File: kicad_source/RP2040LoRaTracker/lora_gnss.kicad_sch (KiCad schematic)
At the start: 16 parts, among them U2 Ai-Thinker-Ra-01, U3 NEO-M8N, U5 24LC32

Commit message: started layout
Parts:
- U5: footprint (none) -> Package_SO:TSSOP-8_4.4x3mm_P0.65mm
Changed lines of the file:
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@@
 			)
 		)
-		(property "Footprint" ""
+		(property "Footprint" "Package_SO:TSSOP-8_4.4x3mm_P0.65mm"
 			(at 41.91 128.27 0)
 			(effects

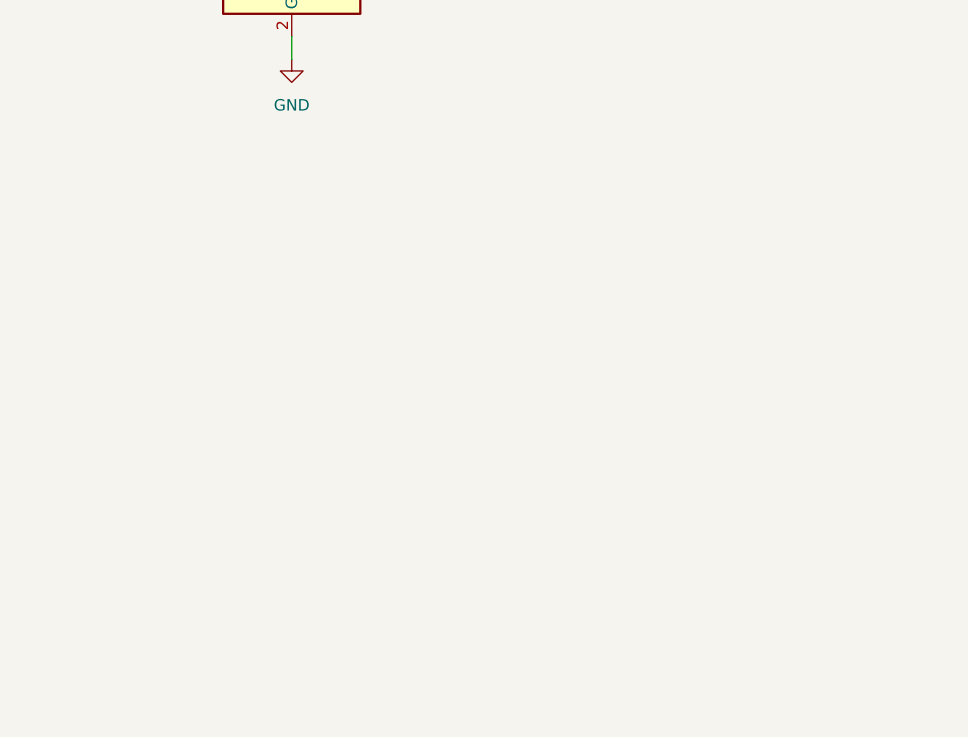
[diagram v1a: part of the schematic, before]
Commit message: added BME280 and quiic connector
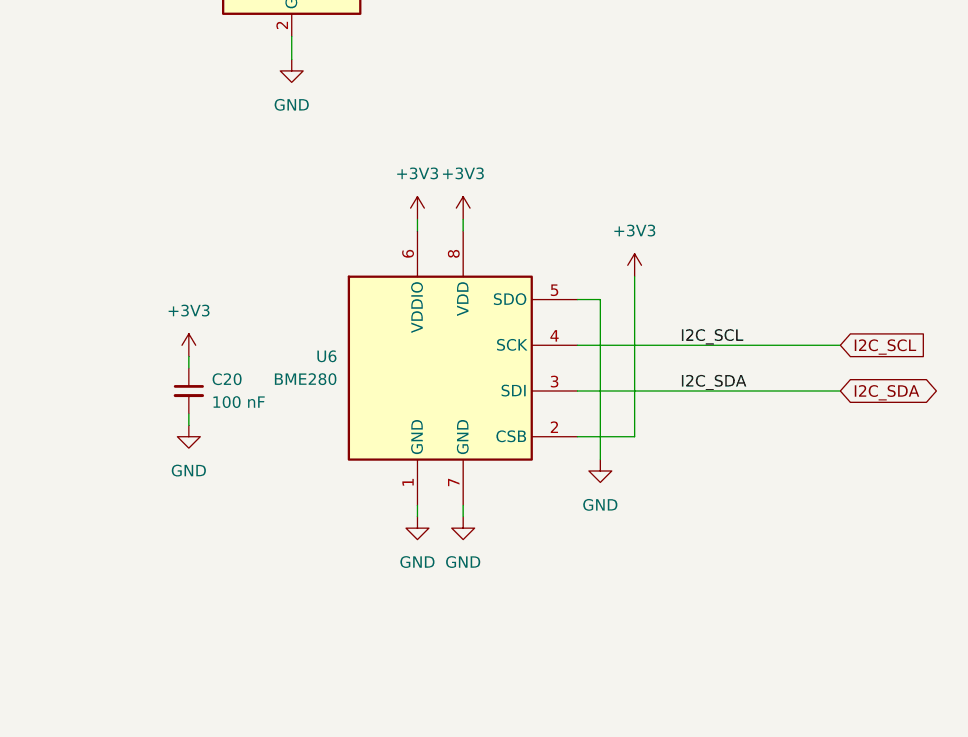
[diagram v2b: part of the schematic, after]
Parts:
- added C20: 100 nF, Capacitor_SMD:C_0603_1608Metric, symbol Device:C_Small
- added U6: BME280, Package_LGA:Bosch_LGA-8_2.5x2.5mm_P0.65mm_ClockwisePinNumbering, symbol Sensor:BME280
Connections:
- net +3V3: now also C20.1, U6.2 (CSB), U6.6 (VDDIO), U6.8 (VDD)
- net GND: now also C20.2, U6.1 (GND), U6.5 (SDO), U6.7 (GND)
- new net I2C_SCL: U6.4 (SCK)
- new net I2C_SDA: U6.3 (SDI)

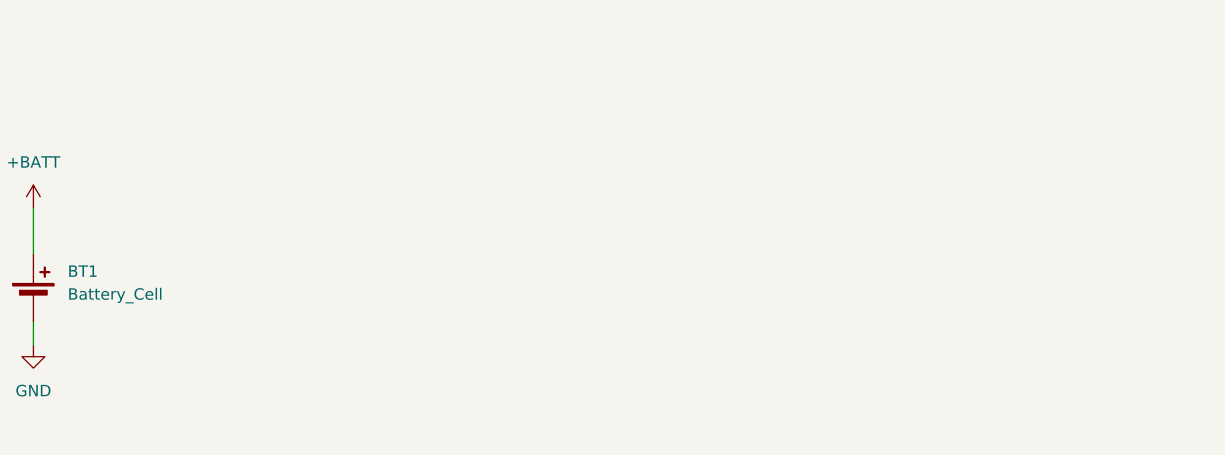
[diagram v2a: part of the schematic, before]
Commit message: added voltage regulator
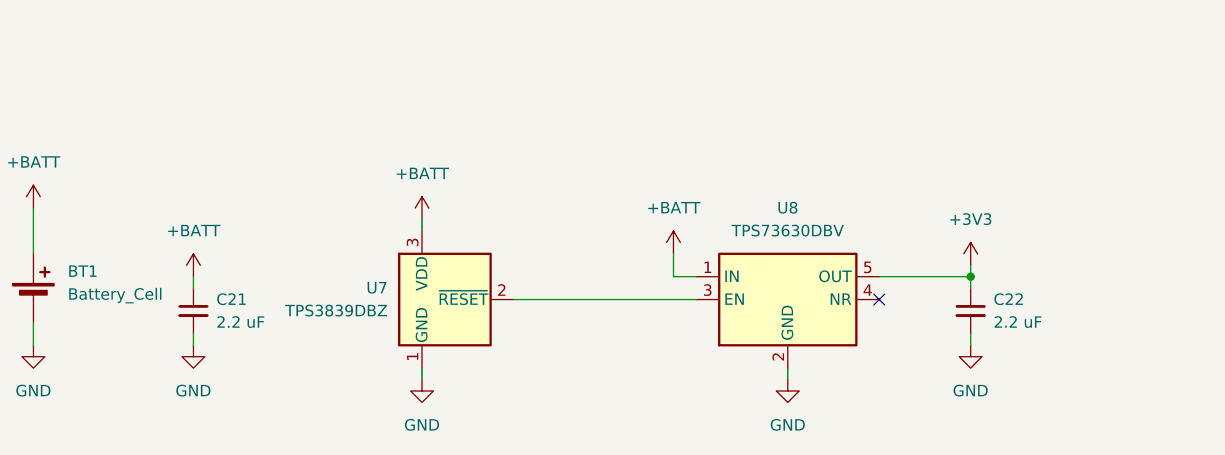
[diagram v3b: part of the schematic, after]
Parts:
- added C21, C22: 2.2 uF, Capacitor_SMD:C_0603_1608Metric, symbol Device:C_Small
- added U7: TPS3839DBZ, Package_TO_SOT_SMD:SOT-23, symbol Power_Supervisor:TPS3839DBZ
- added U8: TPS73630DBV, Package_TO_SOT_SMD:SOT-23-5, symbol Regulator_Linear:TPS73630DBV
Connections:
- net +3V3: now also C22.1, U8.5 (OUT)
- net +BATT: now also C21.1, U7.3 (VDD), U8.1 (IN)
- net GND: now also C21.2, C22.2, U7.1 (GND), U8.2 (GND)
- new net: U7.2 (~{RESET}), U8.3 (EN)
- no-connect marks 11 -> 12

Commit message: added battery charger
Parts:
- added C23: 2.2 uF, Capacitor_SMD:C_0603_1608Metric, symbol Device:C_Small
- added D3: LED_Small, LED_SMD:LED_0603_1608Metric, symbol Device:LED_Small
- added D4: MBR120, Diode_SMD:D_SOD-123, symbol Device:D_Schottky_Small
- added Q1: NTR4171P, Package_TO_SOT_SMD:SOT-23, symbol Device:Q_PMOS_GSD
- added R14, R16: 4k7, Resistor_SMD:R_0603_1608Metric, symbol Device:R_Small
- added R15: 10k, Resistor_SMD:R_0603_1608Metric, symbol Device:R_Small
- added U9: MCP73832-2-OT, Package_TO_SOT_SMD:SOT-23-5, symbol Battery_Management:MCP73832-2-OT
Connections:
- net +BATT: now also Q1.3 (D), U9.3 (V_{BAT}); no longer C21.1, U7.3 (VDD), U8.1 (IN)
- net GND: now also C23.2, R15.1, U9.2 (V_{SS})
- new net: R14.1, U9.1 (STAT)
- new net: D3.1 (K), R14.2
- new net: R15.2, U9.5 (PROG)
- new net: Q1.1 (G), R16.1
- new net VBUS: C23.1, D3.2 (A), D4.2 (A), R16.2, U9.4 (V_{DD})
- new net VCC: C21.1, D4.1 (K), Q1.2 (S), U7.3 (VDD), U8.1 (IN)
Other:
- note added: "AI-Thinker Ra-01 LoRa module"
- note added: "Bosch BME280 environmental sensor"
- note added: "u-Blox NEO-6M or NEO-M8N GNSS receiver"
- moved on the sheet: AE2, D2, L1, R10, R11, R8, R9, U3, U5

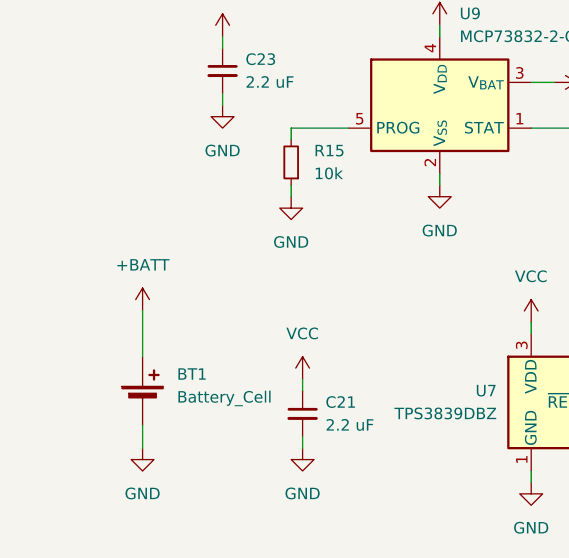
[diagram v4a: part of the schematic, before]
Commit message: changed battery holder, updated layout
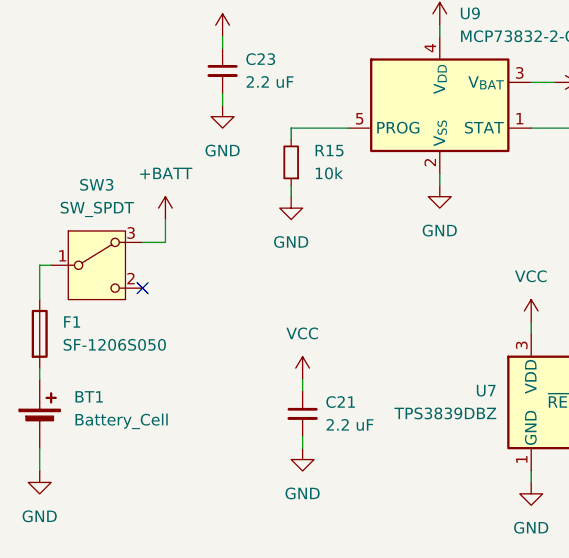
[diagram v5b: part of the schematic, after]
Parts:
- added F1: SF-1206S050, Fuse:Fuse_1206_3216Metric, symbol Device:Fuse
- added SW3: SW_SPDT, Button_Switch_THT:SW_Slide-03_Wuerth-WS-SLTV_10x2.5x6.4_P2.54mm, symbol Switch:SW_SPDT_312
- BT1: footprint Battery:BatteryHolder_Keystone_1042_1x18650 -> generationmake:KEYSTONE_1043
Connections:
- net +BATT: now also SW3.3 (A); no longer BT1.1 (+)
- new net: BT1.1 (+), F1.2
- new net: F1.1, SW3.1 (B)
- no-connect marks 12 -> 13
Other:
- moved on the sheet: BT1
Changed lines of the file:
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@@
 	)
 	(no_connect
+		(at 26.67 167.64)
+	)
+	(no_connect
 		(at 215.9 81.28)
 	)
@@
 	(wire
 		(pts
+			(xy 26.67 162.56) (xy 29.21 162.56)
+		)
+		(stroke
+			(width 0)
+			(type default)
+		)
+	)
+	(wire
+		(pts
 			(xy 109.22 147.32) (xy 113.03 147.32)
 		)
@@
 	(wire
 		(pts
+			(xy 29.21 162.56) (xy 29.21 160.02)
+		)
+		(stroke
+			(width 0)
+			(type default)
+		)
+	)
+	(wire
+		(pts
 			(xy 19.05 105.41) (xy 19.05 107.95)
 		)
@@
 	(wire
 		(pts
+			(xy 15.24 176.53) (xy 15.24 177.8)
+		)
+		(stroke
+			(width 0)
+			(type default)
+		)
+	)
+	(wire
+		(pts
 			(xy 205.74 91.44) (xy 205.74 93.98)
 		)
@@
 	(wire
 		(pts
-			(xy 26.67 182.88) (xy 26.67 185.42)
+			(xy 15.24 185.42) (xy 15.24 187.96)
 		)
 		(stroke
@@
 	(wire
 		(pts
-			(xy 26.67 170.18) (xy 26.67 175.26)
+			(xy 15.24 168.91) (xy 15.24 165.1)
 		)
 		(stroke
@@
 	(wire
 		(pts
+			(xy 15.24 165.1) (xy 16.51 165.1)
+		)
+		(stroke
+			(width 0)
+			(type default)
+		)
+	)
+	(wire
+		(pts
 			(xy 41.91 105.41) (xy 60.96 105.41)
 		)
@@
 	(symbol
 		(lib_id "Device:Battery_Cell")
-		(at 26.67 180.34 0)
+		(at 15.24 182.88 0)
 		(unit 1)
 		(exclude_from_sim no)
@@
 		(fields_autoplaced yes)
 		(property "Reference" "BT1"
-			(at 30.48 177.2284 0)
+			(at 19.05 179.7684 0)
 			(effects
 				(font
@@
 		)
 		(property "Value" "Battery_Cell"
-			(at 30.48 179.7684 0)
+			(at 19.05 182.3084 0)
 			(effects
 				(font
@@
 			)
 		)
-		(property "Footprint" "Battery:BatteryHolder_Keystone_1042_1x18650"
-			(at 26.67 178.816 90)
+		(property "Footprint" "generationmake:KEYSTONE_1043"
+			(at 15.24 181.356 90)
 			(effects
 				(font
@@
 		)
 		(property "Datasheet" "~"
-			(at 26.67 178.816 90)
+			(at 15.24 181.356 90)
 			(effects
 				(font
@@
 		)
 		(property "Description" "Single-cell battery"
-			(at 26.67 180.34 0)
+			(at 15.24 182.88 0)
 			(effects
 				(font
@@
 	(symbol
 		(lib_id "power:GND")
-		(at 26.67 185.42 0)
+		(at 15.24 187.96 0)
 		(unit 1)
 		(exclude_from_sim no)
@@
 		(fields_autoplaced yes)
 		(property "Reference" "#PWR54"
-			(at 26.67 191.77 0)
+			(at 15.24 194.31 0)
 			(effects
 				(font
@@
 		)
 		(property "Value" "GND"
-			(at 26.67 190.5 0)
+			(at 15.24 193.04 0)
 			(effects
 				(font
@@
 		)
 		(property "Footprint" ""
-			(at 26.67 185.42 0)
+			(at 15.24 187.96 0)
 			(effects
 				(font
@@
 		)
 		(property "Datasheet" ""
-			(at 26.67 185.42 0)
+			(at 15.24 187.96 0)
 			(effects
 				(font
@@
 		)
 		(property "Description" "Power symbol creates a global label with name \"GND\" , ground"
-			(at 26.67 185.42 0)
+			(at 15.24 187.96 0)
 			(effects
 				(font
@@
 	(symbol
 		(lib_id "power:+BATT")
-		(at 26.67 170.18 0)
+		(at 29.21 160.02 0)
 		(unit 1)
 		(exclude_from_sim no)
@@
 		(fields_autoplaced yes)
 		(property "Reference" "#PWR55"
-			(at 26.67 173.99 0)
+			(at 29.21 163.83 0)
 			(effects
 				(font
@@
 		)
 		(property "Value" "+BATT"
-			(at 26.67 165.1 0)
+			(at 29.21 154.94 0)
 			(effects
 				(font
@@
 		)
 		(property "Footprint" ""
-			(at 26.67 170.18 0)
+			(at 29.21 160.02 0)
 			(effects
 				(font
@@
 		)
 		(property "Datasheet" ""
-			(at 26.67 170.18 0)
+			(at 29.21 160.02 0)
 			(effects
 				(font
@@
 		)
 		(property "Description" "Power symbol creates a global label with name \"+BATT\""
-			(at 26.67 170.18 0)
+			(at 29.21 160.02 0)
 			(effects
 				(font
@@
 	)
 	(symbol
+		(lib_id "Device:Fuse")
+		(at 15.24 172.72 0)
+		(unit 1)
+		(exclude_from_sim no)
+		(in_bom yes)
+		(on_board yes)
+		(dnp no)
+		(fields_autoplaced yes)
+		(property "Reference" "F1"
+			(at 17.78 171.4499 0)
+			(effects
+				(font
+					(size 1.27 1.27)
+				)
+				(justify left)
+			)
+		)
+		(property "Value" "SF-1206S050"
+			(at 17.78 173.9899 0)
+			(effects
+				(font
+					(size 1.27 1.27)
+				)
+				(justify left)
+			)
+		)
+		(property "Footprint" "Fuse:Fuse_1206_3216Metric"
+			(at 13.462 172.72 90)
+			(effects
+				(font
+					(size 1.27 1.27)
+				)
+				(hide yes)
+			)
+		)
+		(property "Datasheet" "~"
+			(at 15.24 172.72 0)
+			(effects
+				(font
+					(size 1.27 1.27)
+				)
+				(hide yes)
+			)
+		)
+		(property "Description" "Fuse"
+			(at 15.24 172.72 0)
+			(effects
+				(font
+					(size 1.27 1.27)
+				)
+				(hide yes)
+			)
+		)
+		(pin "2"
+		)
+		(pin "1"
+		)
+		(instances
+			(project ""
+				(path "/143f7a5b-9016-4d2c-b741-f535648590f8/eaeb2dbb-82d1-4bb1-aa6e-4edb004b54b5"
+					(reference "F1")
+					(unit 1)
+				)
+			)
+		)
+	)
+	(symbol
 		(lib_id "power:GND")
 		(at 35.56 147.32 0)
@@
 					(unit 1)
 				)
+			)
+		)
+	)
+	(symbol
+		(lib_id "Switch:SW_SPDT_312")
+		(at 21.59 165.1 0)
+		(unit 1)
+		(exclude_from_sim no)
+		(in_bom yes)
+		(on_board yes)
+		(dnp no)
+		(fields_autoplaced yes)
+		(property "Reference" "SW3"
+			(at 21.59 156.21 0)
+			(effects
+				(font
+					(size 1.27 1.27)
+				)
+			)
+		)
+		(property "Value" "SW_SPDT"
+			(at 21.59 158.75 0)
+			(effects
+				(font
+					(size 1.27 1.27)
+				)
+			)
+		)
+		(property "Footprint" "Button_Switch_THT:SW_Slide-03_Wuerth-WS-SLTV_10x2.5x6.4_P2.54mm"
+			(at 21.59 175.26 0)
+			(effects
+				(font
+					(size 1.27 1.27)
+				)
+				(hide yes)
+			)
+		)
+		(property "Datasheet" "~"
+			(at 21.59 172.72 0)
+			(effects
+				(font
+					(size 1.27 1.27)
+				)
+				(hide yes)
+			)
+		)
+		(property "Description" "Switch, single pole double throw"
+			(at 21.59 165.1 0)
+			(effects
+				(font
+					(size 1.27 1.27)
+				)
+				(hide yes)
+			)
+		)
+		(pin "3"
+		)
+		(pin "2"
+		)
+		(pin "1"
+		)
+		(instances
+			(project ""
+				(path "/143f7a5b-9016-4d2c-b741-f535648590f8/eaeb2dbb-82d1-4bb1-aa6e-4edb004b54b5"
+					(reference "SW3")
+					(unit 1)
+				)

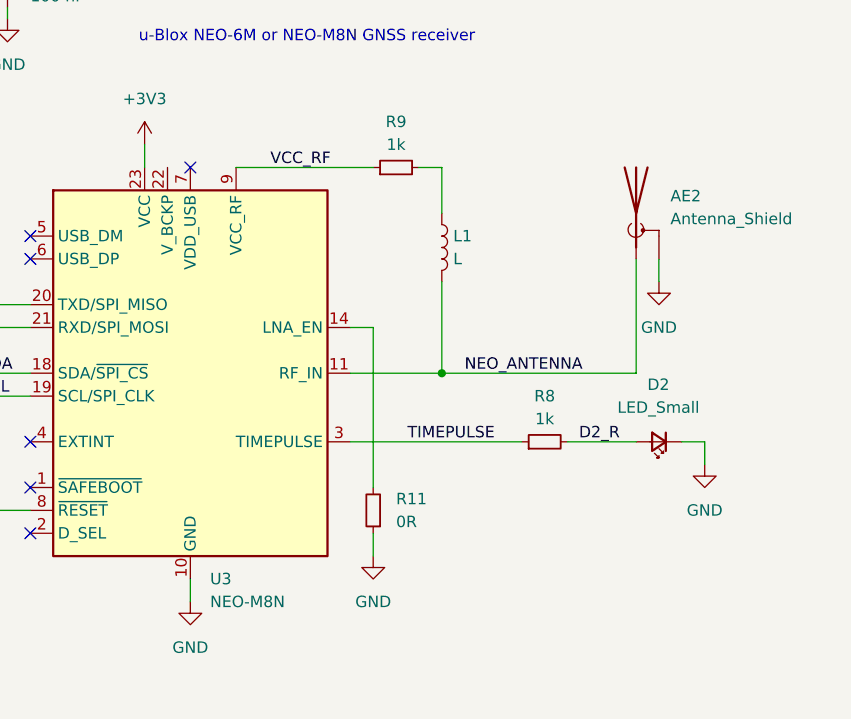
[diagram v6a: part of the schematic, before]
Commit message: updated some values in schematic, added comments, updated schematic pdf
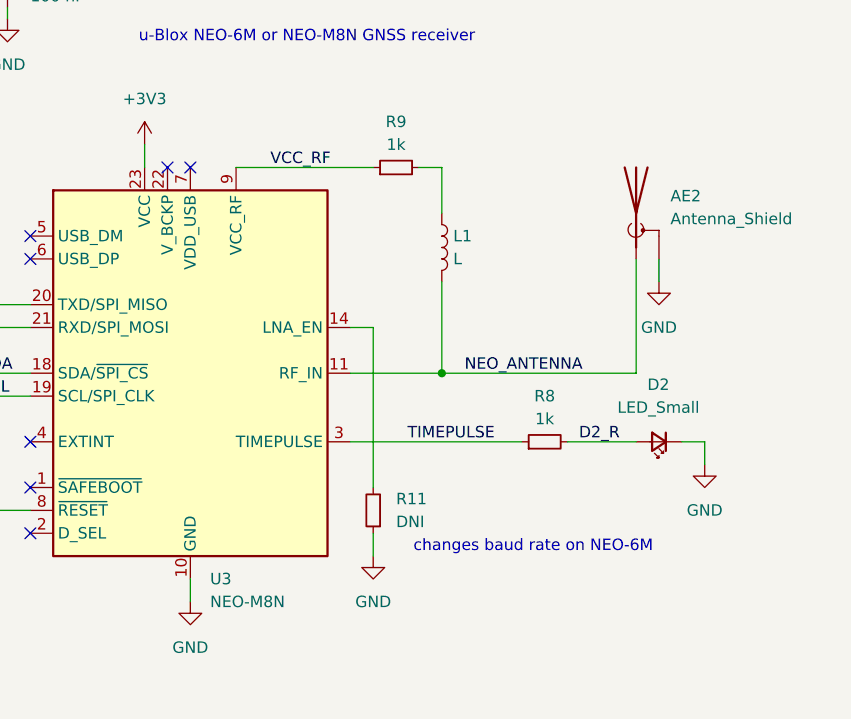
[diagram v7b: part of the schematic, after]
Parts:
- R11: value 0R -> DNI
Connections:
- no-connect marks 13 -> 14
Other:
- note added: "changes baud rate on NEO-6M"
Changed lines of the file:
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@@
 	(title_block
 		(title "RP2040LoRaTracker")
-		(date "2025-04-01")
+		(date "2025-04-20")
 		(rev "0.1")
 		(company "generationmake")
@@
 	)
 	(no_connect
+		(at 85.09 50.8)
+	)
+	(no_connect
 		(at 215.9 76.2)
 	)
@@
 			(width 0)
 			(type default)
+		)
+	)
+	(text "changes baud rate on NEO-6M"
+		(exclude_from_sim no)
+		(at 125.73 92.964 0)
+		(effects
+			(font
+				(size 1.27 1.27)
+			)
 		)
 	)
@@
 			)
 		)
-		(property "Value" "0R"
+		(property "Value" "DNI"
 			(at 110.49 90.1699 0)
 			(effects

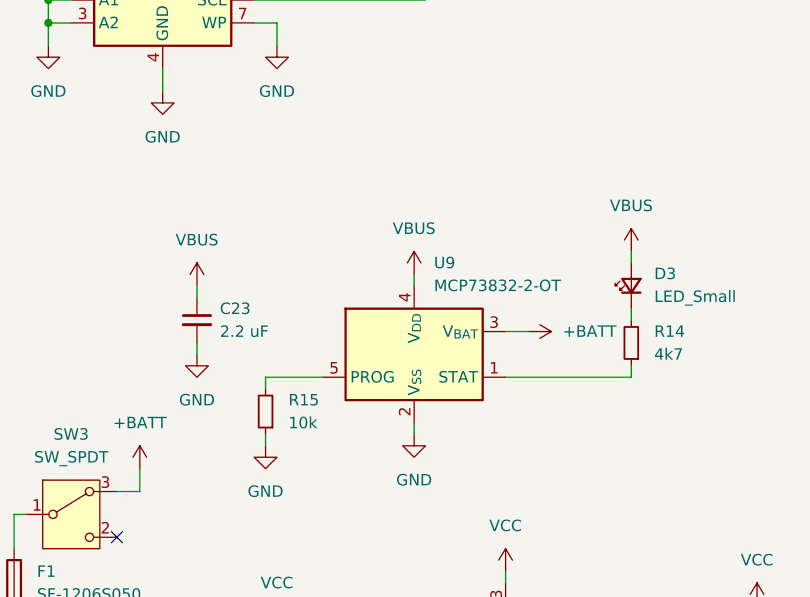
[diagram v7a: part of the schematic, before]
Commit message: set charging current to 500 mA (R15=2k)
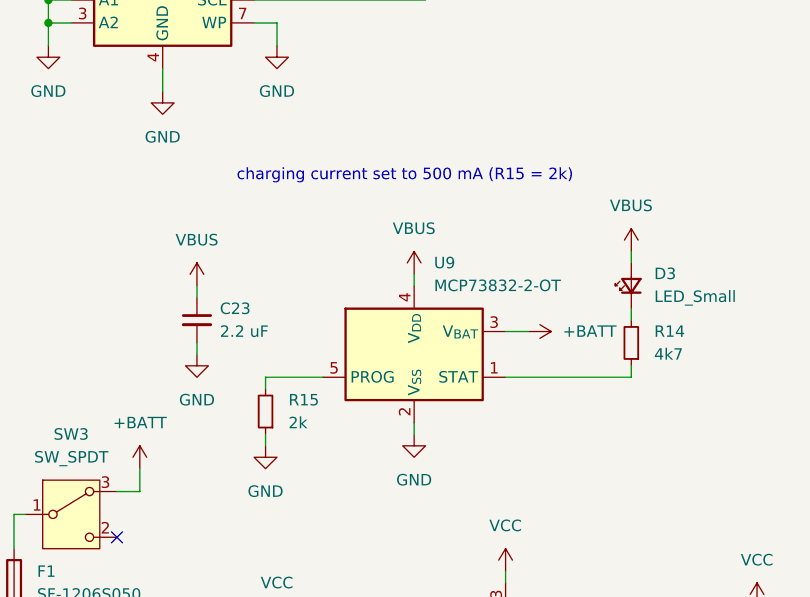
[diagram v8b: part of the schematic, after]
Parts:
- R15: value 10k -> 2k
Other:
- note added: "charging current set to 500 mA (R15 = 2k)"
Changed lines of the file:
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@@
 	(title_block
 		(title "RP2040LoRaTracker")
-		(date "2025-04-20")
+		(date "2025-05-04")
 		(rev "0.1")
 		(company "generationmake")
@@
 		)
 	)
+	(text "charging current set to 500 mA (R15 = 2k)"
+		(exclude_from_sim no)
+		(at 58.674 127.508 0)
+		(effects
+			(font
+				(size 1.27 1.27)
+			)
+		)
+	)
 	(text "Bosch BME280 environmental sensor"
 		(exclude_from_sim no)
@@
 			)
 		)
-		(property "Value" "10k"
+		(property "Value" "2k"
 			(at 45.72 154.9399 0)
 			(effects
